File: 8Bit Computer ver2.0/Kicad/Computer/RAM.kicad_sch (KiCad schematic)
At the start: 4 parts, among them IC186 SN74AHC74DR, IC187 SN74LVC1G14DBVR, IC188 SN74LVC1G14DBVR, IC58 AS7C1024B-12TCN

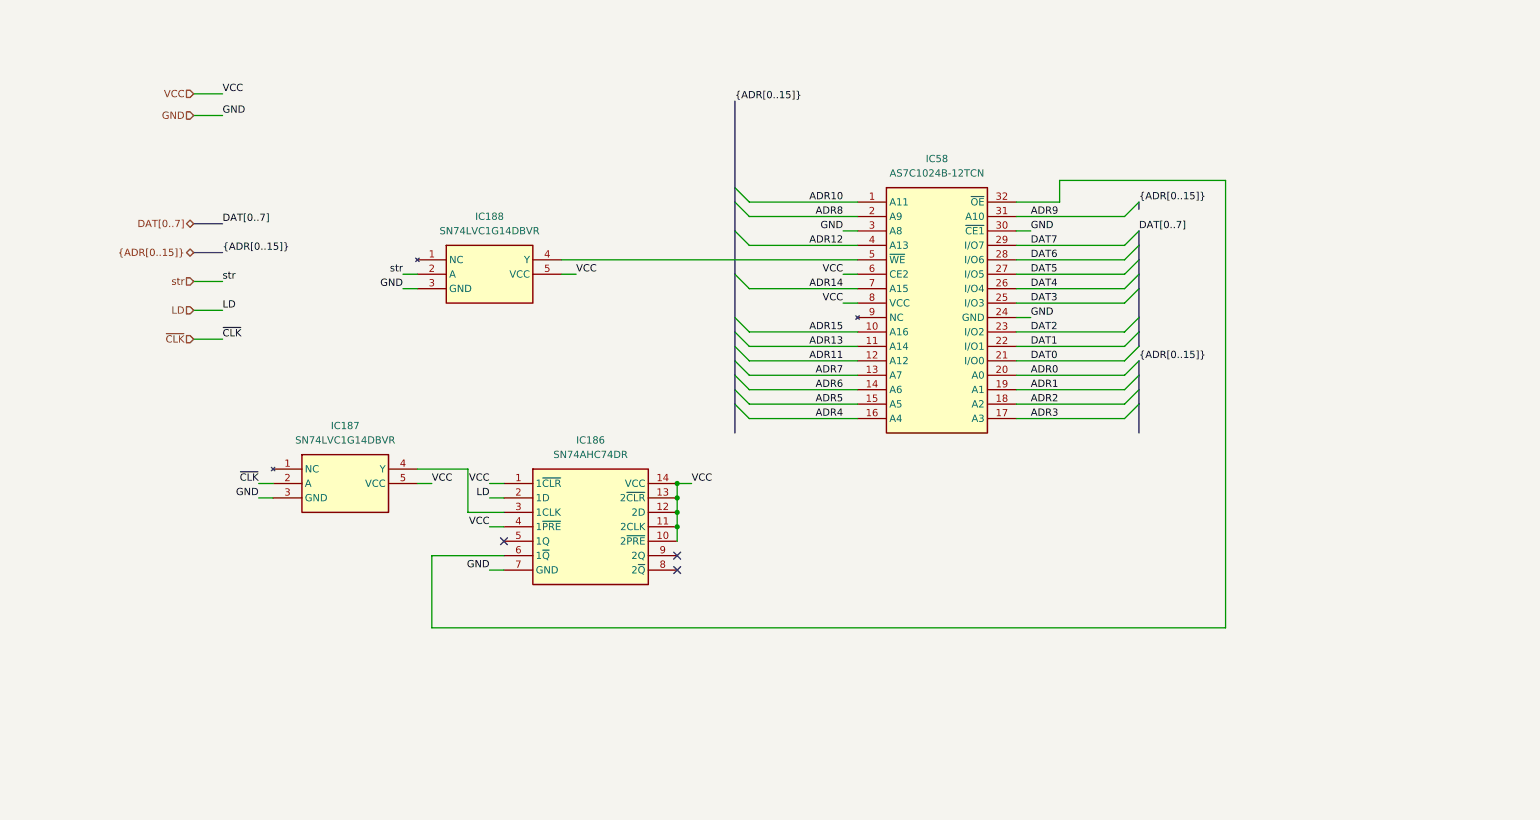
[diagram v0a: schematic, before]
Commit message: Kicad, parts
parts:
added USB C PD Triggerboard
added Delay Chip for 90ns
added Push Button
Kicad:
added USB C PD Triggerboard
added rising edge detector via Delay and Xor for Accept Push Button
added VBUS net
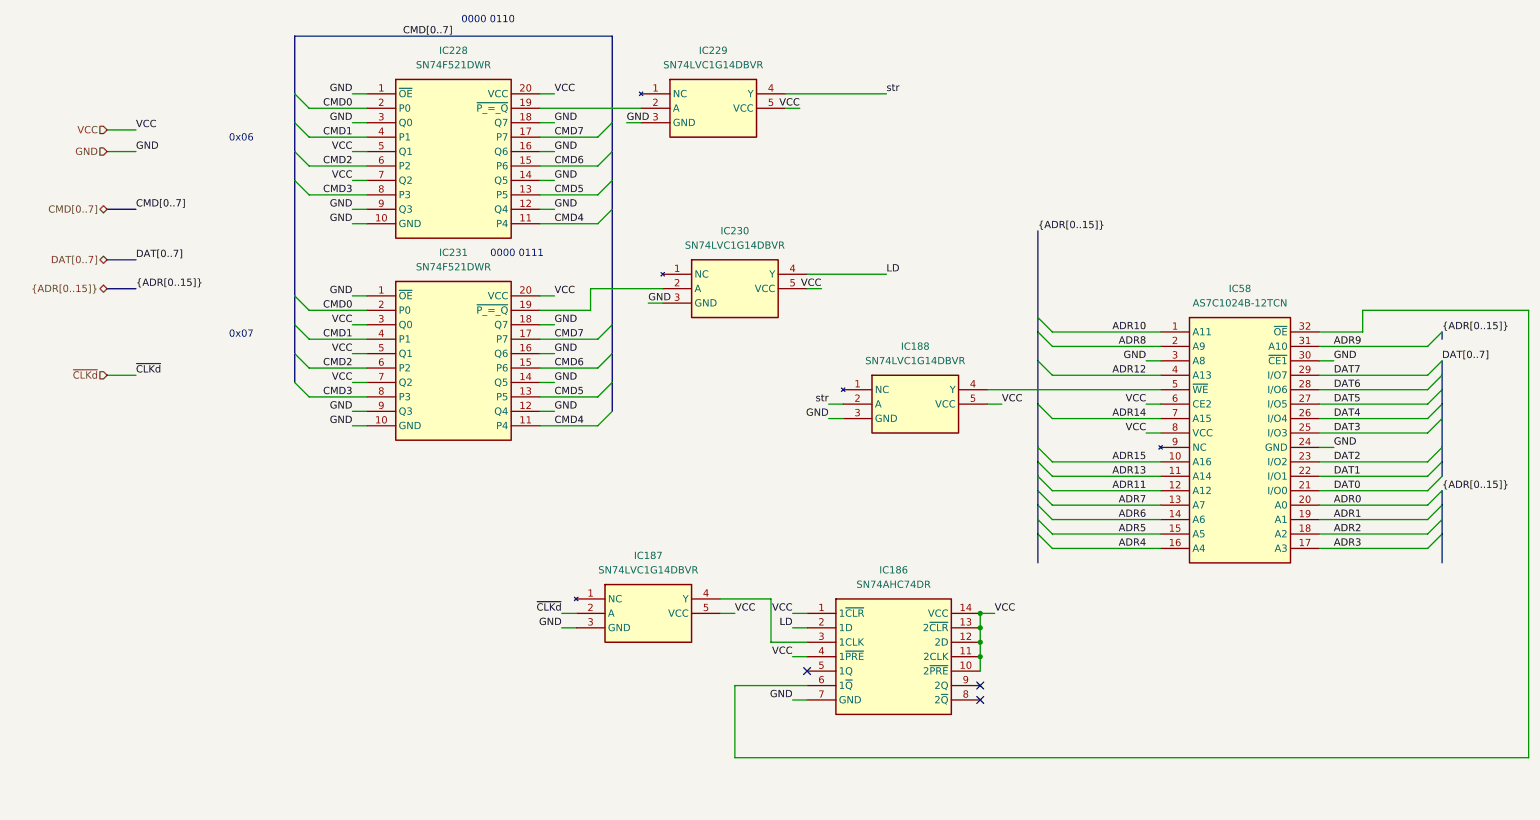
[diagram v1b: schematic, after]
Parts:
- added IC228, IC231: SN74F521DWR, Samacsys:SOIC127P1030X265-20N, symbol Samacsys:SN74F521DWR
- added IC229, IC230: SN74LVC1G14DBVR, Samacsys:SOT95P280X145-5N, symbol Samacsys:SN74LVC1G14DBVR
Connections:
- net GND: now also IC228.1 (~{OE}), IC228.10 (GND), IC228.12 (Q4), IC228.14 (Q5), IC228.16 (Q6), IC228.18 (Q7), IC228.3 (Q0), IC228.9 (Q3), IC229.3 (GND), IC230.3 (GND), IC231.1 (~{OE}), IC231.10 (GND), IC231.12 (Q4), IC231.14 (Q5), IC231.16 (Q6), IC231.18 (Q7), IC231.9 (Q3)
- net LD: now also IC230.4 (Y)
- net VCC: now also IC228.20 (VCC), IC228.5 (Q1), IC228.7 (Q2), IC229.5 (VCC), IC230.5 (VCC), IC231.20 (VCC), IC231.3 (Q0), IC231.5 (Q1), IC231.7 (Q2)
- net str: now also IC229.4 (Y)
- net ~{CLK} renamed ~{CLKd}
- new net: IC230.2 (A), IC231.19 (~{P_=_Q})
- new net: IC228.19 (~{P_=_Q}), IC229.2 (A)
- new net CMD0: IC228.2 (P0), IC231.2 (P0)
- new net CMD1: IC228.4 (P1), IC231.4 (P1)
- new net CMD2: IC228.6 (P2), IC231.6 (P2)
- new net CMD3: IC228.8 (P3), IC231.8 (P3)
- new net CMD4: IC228.11 (P4), IC231.11 (P4)
- new net CMD5: IC228.13 (P5), IC231.13 (P5)
- new net CMD6: IC228.15 (P6), IC231.15 (P6)
- new net CMD7: IC228.17 (P7), IC231.17 (P7)
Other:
- note added: "0000 0110"
- note added: "0000 0111"
- note added: "0x06"
- note added: "0x07"
- moved on the sheet: IC186, IC187, IC188, IC58

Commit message: Kicad
changed to module version
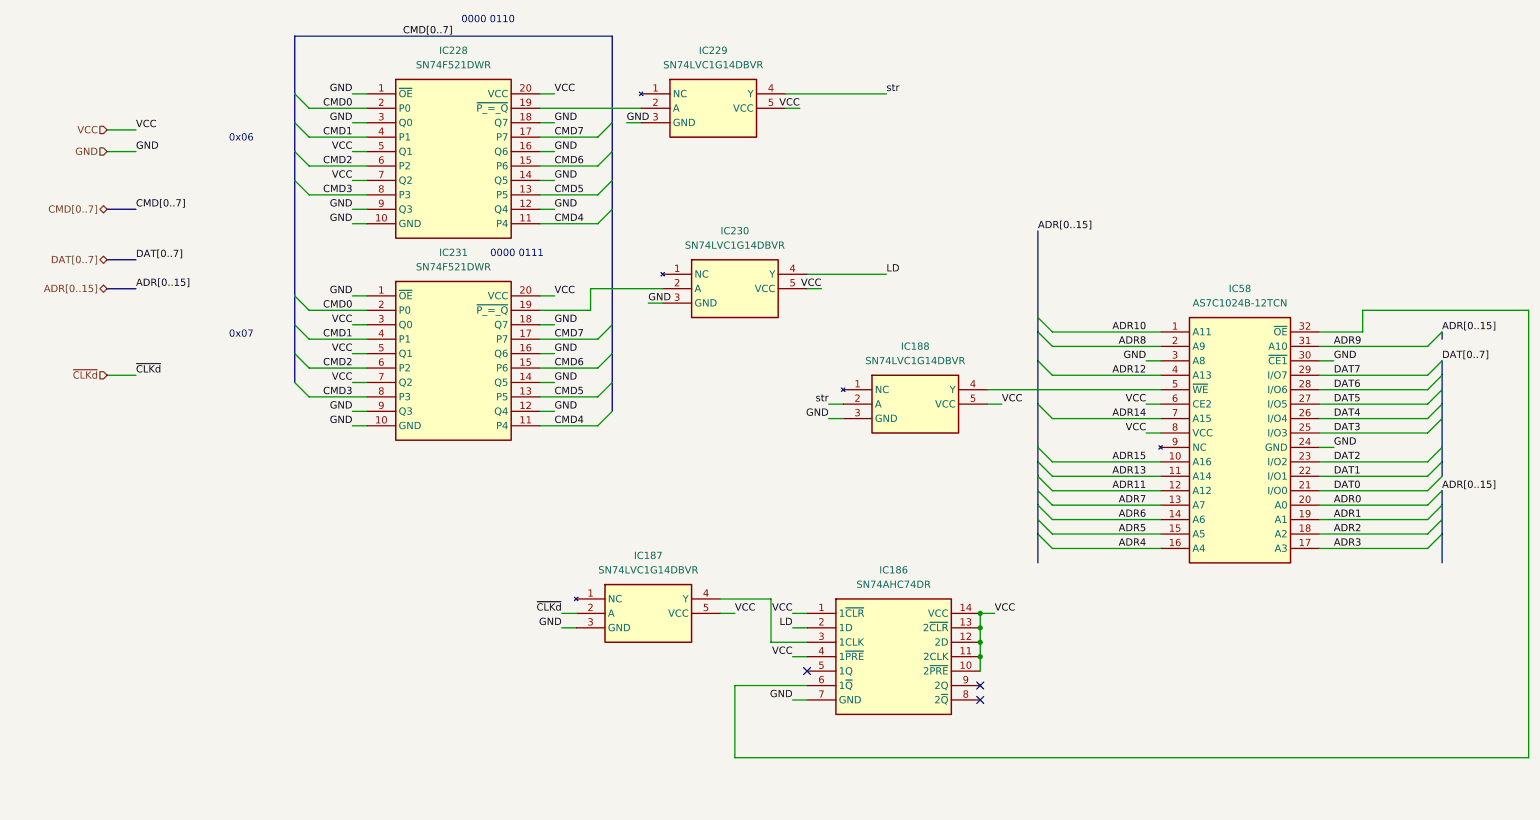
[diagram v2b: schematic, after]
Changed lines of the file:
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@@
 		)
 	)
-	(label "{ADR[0..15]}"
+	(label "ADR[0..15]"
 		(at 194.31 66.04 0)
 		(effects
@@
 		)
 	)
-	(label "{ADR[0..15]}"
+	(label "ADR[0..15]"
 		(at 35.56 76.2 0)
 		(effects
@@
 		)
 	)
-	(label "{ADR[0..15]}"
+	(label "ADR[0..15]"
 		(at 265.43 111.76 0)
 		(effects
@@
 		)
 	)
-	(label "{ADR[0..15]}"
+	(label "ADR[0..15]"
 		(at 265.43 83.82 0)
 		(effects
@@
 		)
 	)
-	(hierarchical_label "{ADR[0..15]}"
+	(hierarchical_label "ADR[0..15]"
 		(shape tri_state)
 		(at 30.48 76.2 180)

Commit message: Kicad SCH/PCB
Kicad SCH/PCB:
changed the References in SCH
began with INOUTPUT module nearly done
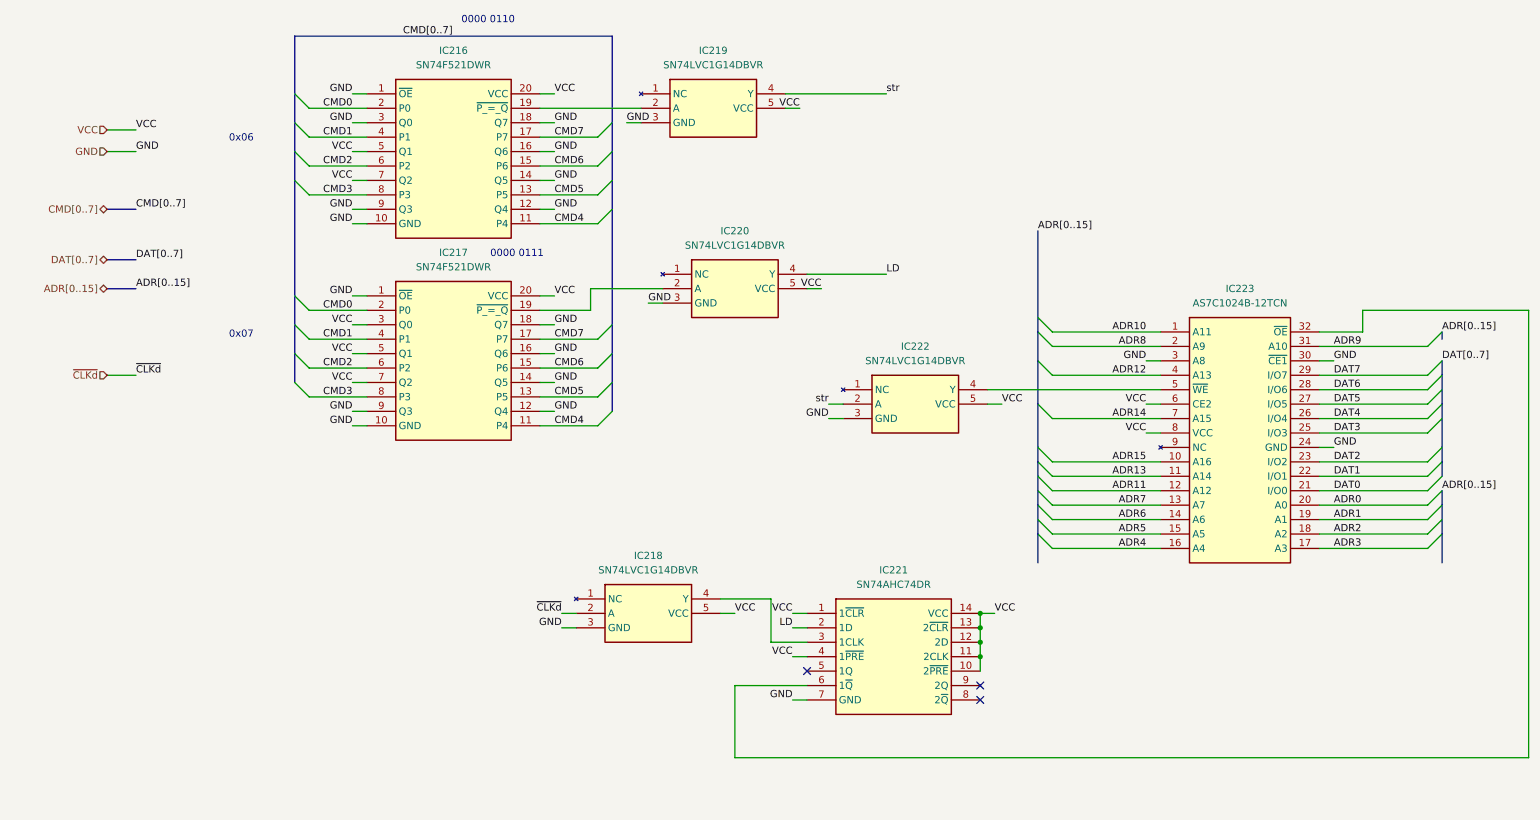
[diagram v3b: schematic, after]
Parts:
- renumbered IC228 to IC216, IC231 to IC217, IC187 to IC218, IC229 to IC219, IC230 to IC220, IC186 to IC221, IC188 to IC222, IC58 to IC223
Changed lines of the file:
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@@
 		(dnp no)
 		(fields_autoplaced yes)
-		(property "Reference" "IC187"
+		(property "Reference" "IC218"
 			(at 125.73 123.19 0)
 			(effects
@@
 			(project ""
 				(path "/1196a00e-6878-4d6d-82b7-9e052dfe7c14/42d222c2-85ce-47c7-bf35-977080c4de05"
-					(reference "IC187")
+					(reference "IC218")
 					(unit 1)
 				)
@@
 		(dnp no)
 		(fields_autoplaced yes)
-		(property "Reference" "IC186"
+		(property "Reference" "IC221"
 			(at 168.91 125.73 0)
 			(effects
@@
 			(project ""
 				(path "/1196a00e-6878-4d6d-82b7-9e052dfe7c14/42d222c2-85ce-47c7-bf35-977080c4de05"
-					(reference "IC186")
+					(reference "IC221")
 					(unit 1)
 				)
@@
 		(dnp no)
 		(fields_autoplaced yes)
-		(property "Reference" "IC231"
+		(property "Reference" "IC217"
 			(at 91.44 69.85 0)
 			(effects
@@
 			(project "Computer"
 				(path "/1196a00e-6878-4d6d-82b7-9e052dfe7c14/42d222c2-85ce-47c7-bf35-977080c4de05"
-					(reference "IC231")
+					(reference "IC217")
 					(unit 1)
 				)
@@
 		(dnp no)
 		(fields_autoplaced yes)
-		(property "Reference" "IC228"
+		(property "Reference" "IC216"
 			(at 91.44 34.29 0)
 			(effects
@@
 			(project "Computer"
 				(path "/1196a00e-6878-4d6d-82b7-9e052dfe7c14/42d222c2-85ce-47c7-bf35-977080c4de05"
-					(reference "IC228")
+					(reference "IC216")
 					(unit 1)
 				)
@@
 		(dnp no)
 		(fields_autoplaced yes)
-		(property "Reference" "IC230"
+		(property "Reference" "IC220"
 			(at 140.97 66.04 0)
 			(effects
@@
 			(project "Computer"
 				(path "/1196a00e-6878-4d6d-82b7-9e052dfe7c14/42d222c2-85ce-47c7-bf35-977080c4de05"
-					(reference "IC230")
+					(reference "IC220")
 					(unit 1)
 				)
@@
 		(dnp no)
 		(fields_autoplaced yes)
-		(property "Reference" "IC229"
+		(property "Reference" "IC219"
 			(at 137.16 34.29 0)
 			(effects
@@
 			(project "Computer"
 				(path "/1196a00e-6878-4d6d-82b7-9e052dfe7c14/42d222c2-85ce-47c7-bf35-977080c4de05"
-					(reference "IC229")
+					(reference "IC219")
 					(unit 1)
 				)
@@
 		(dnp no)
 		(fields_autoplaced yes)
-		(property "Reference" "IC58"
+		(property "Reference" "IC223"
 			(at 229.87 76.2 0)
 			(effects
@@
 			(project ""
 				(path "/1196a00e-6878-4d6d-82b7-9e052dfe7c14/42d222c2-85ce-47c7-bf35-977080c4de05"
-					(reference "IC58")
+					(reference "IC223")
 					(unit 1)
 				)
@@
 		(dnp no)
 		(fields_autoplaced yes)
-		(property "Reference" "IC188"
+		(property "Reference" "IC222"
 			(at 172.72 86.36 0)
 			(effects
@@
 			(project "Computer"
 				(path "/1196a00e-6878-4d6d-82b7-9e052dfe7c14/42d222c2-85ce-47c7-bf35-977080c4de05"
-					(reference "IC188")
+					(reference "IC222")
 					(unit 1)
 				)

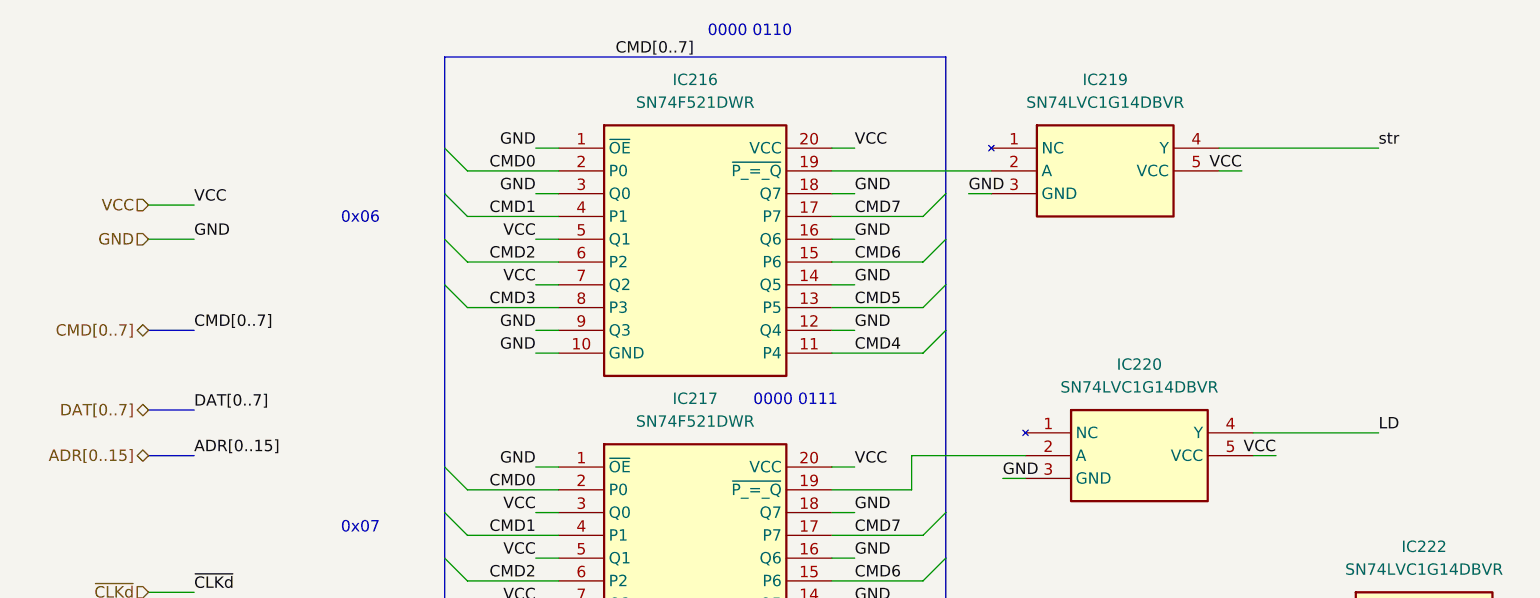
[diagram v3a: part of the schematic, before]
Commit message: Kicad, parts
parts:
added Mux 4:1 for CLK
added LM555
Kicad:
added some Diodes for Flash disable
fixed wrong routing of flag register
fixed wrong routing of STC STF in INC/AddS
LM555 circuit for 1Hz to 100Hz
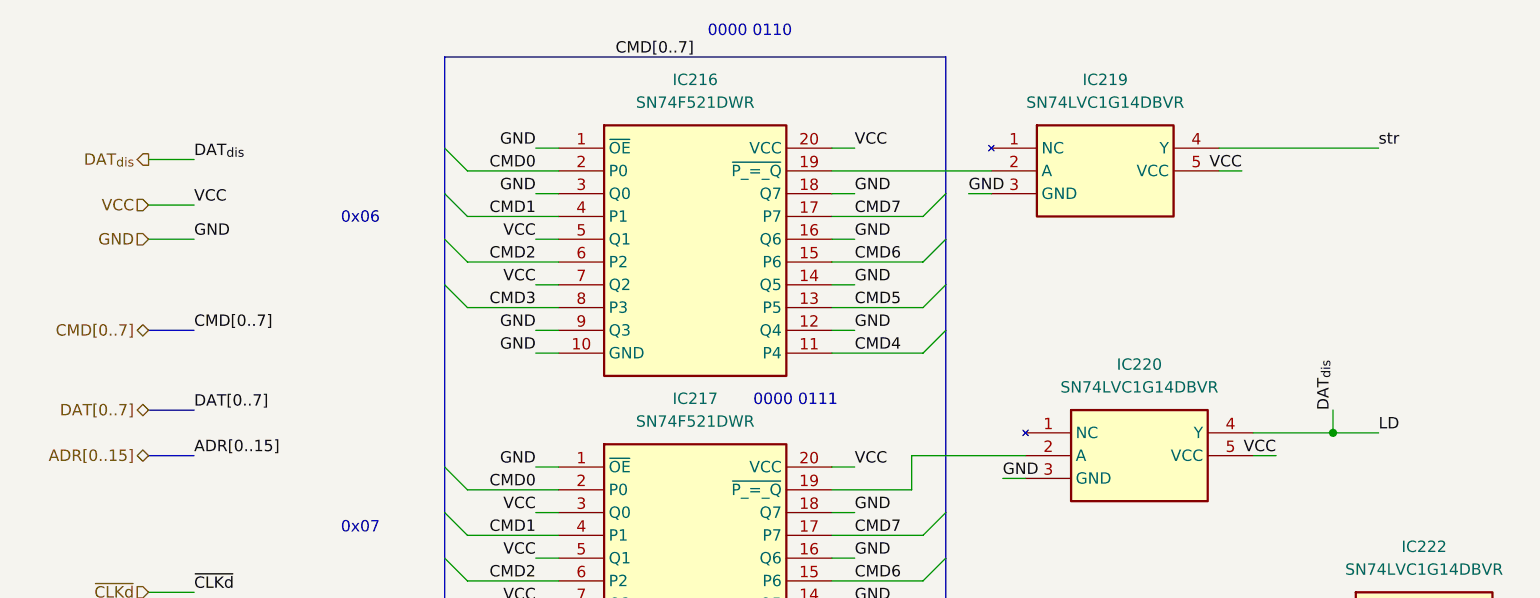
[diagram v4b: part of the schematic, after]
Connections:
- net LD renamed DAT_{dis}
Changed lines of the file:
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@@
+	)
+	(junction
+		(at 162.56 73.66)
+		(diameter 0)
+		(color 0 0 0 0)
 	)
 	(junction
@@
 	(wire
 		(pts
+			(xy 30.48 43.18) (xy 35.56 43.18)
+		)
+		(stroke
+			(width 0)
+			(type default)
+		)
+	)
+	(wire
+		(pts
 			(xy 73.66 100.33) (xy 76.2 100.33)
 		)
@@
 	(wire
 		(pts
-			(xy 153.67 73.66) (xy 167.64 73.66)
+			(xy 153.67 73.66) (xy 162.56 73.66)
 		)
 		(stroke
@@
 	(wire
 		(pts
+			(xy 162.56 73.66) (xy 167.64 73.66)
+		)
+		(stroke
+			(width 0)
+			(type default)
+		)
+	)
+	(wire
+		(pts
 			(xy 243.84 111.76) (xy 262.89 111.76)
 		)
@@
 		(pts
 			(xy 243.84 83.82) (xy 251.46 83.82)
+		)
+		(stroke
+			(width 0)
+			(type default)
+		)
+	)
+	(wire
+		(pts
+			(xy 162.56 71.12) (xy 162.56 73.66)
 		)
 		(stroke
@@
 		)
 	)
+	(label "DAT_{dis}"
+		(at 162.56 71.12 90)
+		(effects
+			(font
+				(size 1.27 1.27)
+			)
+			(justify left bottom)
+		)
+	)
 	(label "CMD7"
 		(at 109.22 85.09 0)
@@
 	(label "DAT[0..7]"
 		(at 265.43 88.9 0)
+		(effects
+			(font
+				(size 1.27 1.27)
+			)
+			(justify left bottom)
+		)
+	)
+	(label "DAT_{dis}"
+		(at 35.56 43.18 0)
 		(effects
 			(font
@@
 		(effects
 			(font
+				(size 1.27 1.27)
+			)
+			(justify right)
+		)
+	)
+	(hierarchical_label "DAT_{dis}"
+		(shape output)
+		(at 30.48 43.18 180)
+		(effects
+			(font
